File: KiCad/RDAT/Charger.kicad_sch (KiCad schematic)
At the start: 52 parts, among them U6 BQ24617RGER

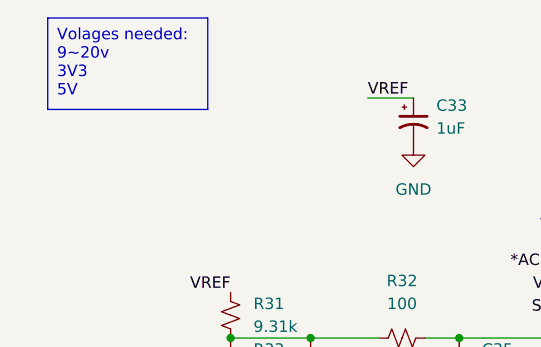
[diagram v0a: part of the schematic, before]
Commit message: Add new notes; update component references in schematics and footprints, and complete charging design
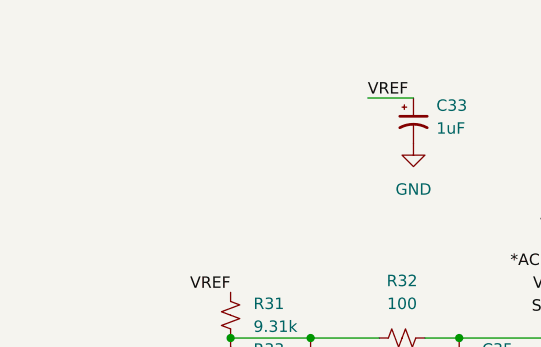
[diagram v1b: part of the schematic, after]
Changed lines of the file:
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@@
 		)
 	)
-	(text_box "Volages needed:\n9~20v\n3V3\n5V"
-		(exclude_from_sim no)
-		(at 15.24 15.24 0)
-		(size 17.78 10.16)
-		(stroke
-			(width 0)
-			(type default)
-		)
-		(fill
-			(type none)
-		)
-		(effects
-			(font
-				(size 1.27 1.27)
-			)
-			(justify left top)
-		)
-	)
 	(text "Q2"
 		(exclude_from_sim no)
@@
 		)
 		(instances
-			(project ""
+			(project "RDAT"
 				(path "/0db9370a-8a21-4fd2-83a9-f207c3725dc9/64601ab1-4b63-421f-a3b9-e484b74e1409"
 					(reference "#PWR052")
@@
 		)
 		(instances
-			(project ""
+			(project "RDAT"
 				(path "/0db9370a-8a21-4fd2-83a9-f207c3725dc9/64601ab1-4b63-421f-a3b9-e484b74e1409"
 					(reference "C35")
@@
 		)
 		(instances
-			(project ""
+			(project "RDAT"
 				(path "/0db9370a-8a21-4fd2-83a9-f207c3725dc9/64601ab1-4b63-421f-a3b9-e484b74e1409"
 					(reference "C42")
@@
 		)
 		(instances
-			(project ""
+			(project "RDAT"
 				(path "/0db9370a-8a21-4fd2-83a9-f207c3725dc9/64601ab1-4b63-421f-a3b9-e484b74e1409"
 					(reference "U6")
@@
 		)
 		(instances
-			(project ""
+			(project "RDAT"
 				(path "/0db9370a-8a21-4fd2-83a9-f207c3725dc9/64601ab1-4b63-421f-a3b9-e484b74e1409"
 					(reference "D111")
@@
 		)
 		(instances
-			(project ""
+			(project "RDAT"
 				(path "/0db9370a-8a21-4fd2-83a9-f207c3725dc9/64601ab1-4b63-421f-a3b9-e484b74e1409"
 					(reference "#PWR051")
@@
 		)
 		(instances
-			(project ""
+			(project "RDAT"
 				(path "/0db9370a-8a21-4fd2-83a9-f207c3725dc9/64601ab1-4b63-421f-a3b9-e484b74e1409"
 					(reference "C36")
@@
 		)
 		(instances
-			(project ""
+			(project "RDAT"
 				(path "/0db9370a-8a21-4fd2-83a9-f207c3725dc9/64601ab1-4b63-421f-a3b9-e484b74e1409"
 					(reference "#PWR050")
@@
 		)
 		(instances
-			(project ""
+			(project "RDAT"
 				(path "/0db9370a-8a21-4fd2-83a9-f207c3725dc9/64601ab1-4b63-421f-a3b9-e484b74e1409"
 					(reference "R33")
@@
 		)
 		(instances
-			(project ""
+			(project "RDAT"
 				(path "/0db9370a-8a21-4fd2-83a9-f207c3725dc9/64601ab1-4b63-421f-a3b9-e484b74e1409"
 					(reference "R32")
@@
 		)
 		(instances
-			(project ""
+			(project "RDAT"
 				(path "/0db9370a-8a21-4fd2-83a9-f207c3725dc9/64601ab1-4b63-421f-a3b9-e484b74e1409"
 					(reference "R43")
@@
 		)
 		(instances
-			(project ""
+			(project "RDAT"
 				(path "/0db9370a-8a21-4fd2-83a9-f207c3725dc9/64601ab1-4b63-421f-a3b9-e484b74e1409"
 					(reference "#PWR053")
@@
 		)
 		(instances
-			(project ""
+			(project "RDAT"
 				(path "/0db9370a-8a21-4fd2-83a9-f207c3725dc9/64601ab1-4b63-421f-a3b9-e484b74e1409"
 					(reference "R45")
@@
 		)
 		(instances
-			(project ""
+			(project "RDAT"
 				(path "/0db9370a-8a21-4fd2-83a9-f207c3725dc9/64601ab1-4b63-421f-a3b9-e484b74e1409"
 					(reference "R47")
@@
 		)
 		(instances
-			(project ""
+			(project "RDAT"
 				(path "/0db9370a-8a21-4fd2-83a9-f207c3725dc9/64601ab1-4b63-421f-a3b9-e484b74e1409"
 					(reference "R46")
@@
 		)
 		(instances
-			(project ""
+			(project "RDAT"
 				(path "/0db9370a-8a21-4fd2-83a9-f207c3725dc9/64601ab1-4b63-421f-a3b9-e484b74e1409"
 					(reference "R_{SR}")
@@
 		)
 		(instances
-			(project ""
+			(project "RDAT"
 				(path "/0db9370a-8a21-4fd2-83a9-f207c3725dc9/64601ab1-4b63-421f-a3b9-e484b74e1409"
 					(reference "D114")
@@
 		)
 		(instances
-			(project ""
+			(project "RDAT"
 				(path "/0db9370a-8a21-4fd2-83a9-f207c3725dc9/64601ab1-4b63-421f-a3b9-e484b74e1409"
 					(reference "TH2")
@@
 		)
 		(instances
-			(project ""
+			(project "RDAT"
 				(path "/0db9370a-8a21-4fd2-83a9-f207c3725dc9/64601ab1-4b63-421f-a3b9-e484b74e1409"
 					(reference "D113")
@@
 		)
 		(instances
-			(project ""
+			(project "RDAT"
 				(path "/0db9370a-8a21-4fd2-83a9-f207c3725dc9/64601ab1-4b63-421f-a3b9-e484b74e1409"
 					(reference "L1")
@@
 		)
 		(instances
-			(project ""
+			(project "RDAT"
 				(path "/0db9370a-8a21-4fd2-83a9-f207c3725dc9/64601ab1-4b63-421f-a3b9-e484b74e1409"
 					(reference "R44")
@@
 		)
 		(instances
-			(project ""
+			(project "RDAT"
 				(path "/0db9370a-8a21-4fd2-83a9-f207c3725dc9/64601ab1-4b63-421f-a3b9-e484b74e1409"
 					(reference "#PWR060")
@@
 		)
 		(instances
-			(project ""
+			(project "RDAT"
 				(path "/0db9370a-8a21-4fd2-83a9-f207c3725dc9/64601ab1-4b63-421f-a3b9-e484b74e1409"
 					(reference "C38")
@@
 		)
 		(instances
-			(project ""
+			(project "RDAT"
 				(path "/0db9370a-8a21-4fd2-83a9-f207c3725dc9/64601ab1-4b63-421f-a3b9-e484b74e1409"
 					(reference "C34")
@@
 		)
 		(instances
-			(project ""
+			(project "RDAT"
 				(path "/0db9370a-8a21-4fd2-83a9-f207c3725dc9/64601ab1-4b63-421f-a3b9-e484b74e1409"
 					(reference "D112")
@@
 		)
 		(instances
-			(project ""
+			(project "RDAT"
 				(path "/0db9370a-8a21-4fd2-83a9-f207c3725dc9/64601ab1-4b63-421f-a3b9-e484b74e1409"
 					(reference "MOSFET3")
@@
 		)
 		(instances
-			(project ""
+			(project "RDAT"
 				(path "/0db9370a-8a21-4fd2-83a9-f207c3725dc9/64601ab1-4b63-421f-a3b9-e484b74e1409"
 					(reference "R31")

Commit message: added volage stuffs
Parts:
- renumbered R_{AC} to R_{AC}1, R_{SR} to R_{SR}1
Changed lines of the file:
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@@
 (kicad_sch
-	(version 20231120)
+	(version 20250114)
 	(generator "eeschema")
-	(generator_version "8.0")
+	(generator_version "9.0")
 	(paper "USLetter" portrait)
 	(title_block
 		(rev "0")
 	)
+	(text "Q2"
+		(exclude_from_sim no)
+		(at 187.706 153.416 0)
+		(effects
+			(font
+				(size 1.27 1.27)
+			)
+		)
+	)
+	(text "Q1"
+		(exclude_from_sim no)
+		(at 53.594 212.598 0)
+		(effects
+			(font
+				(size 1.27 1.27)
+			)
+		)
+	)
+	(text "Q1"
+		(exclude_from_sim no)
+		(at 114.554 212.598 0)
+		(effects
+			(font
+				(size 1.27 1.27)
+			)
+		)
+	)
 	(junction
 		(at 149.86 66.04)
@@
 		)
 	)
-	(text "Q2"
-		(exclude_from_sim no)
-		(at 187.706 153.416 0)
-		(effects
-			(font
-				(size 1.27 1.27)
-			)
-		)
-	)
-	(text "Q1"
-		(exclude_from_sim no)
-		(at 53.594 212.598 0)
-		(effects
-			(font
-				(size 1.27 1.27)
-			)
-		)
-	)
-	(text "Q1"
-		(exclude_from_sim no)
-		(at 114.554 212.598 0)
-		(effects
-			(font
-				(size 1.27 1.27)
-			)
-		)
-	)
 	(label "PH"
 		(at 129.54 172.72 0)
@@
 		(on_board yes)
 		(dnp no)
-		(property "Reference" "R_{AC}"
+		(property "Reference" "R_{AC}1"
 			(at 156.21 195.5801 0)
 			(effects
@@
 			(project "RDAT"
 				(path "/0db9370a-8a21-4fd2-83a9-f207c3725dc9/64601ab1-4b63-421f-a3b9-e484b74e1409"
-					(reference "R_{AC}")
+					(reference "R_{AC}1")
 					(unit 1)
 				)
@@
 		(dnp no)
 		(fields_autoplaced yes)
-		(property "Reference" "R_{SR}"
+		(property "Reference" "R_{SR}1"
 			(at 148.59 163.83 90)
 			(effects
@@
 			(project "RDAT"
 				(path "/0db9370a-8a21-4fd2-83a9-f207c3725dc9/64601ab1-4b63-421f-a3b9-e484b74e1409"
-					(reference "R_{SR}")
+					(reference "R_{SR}1")
 					(unit 1)
 				)

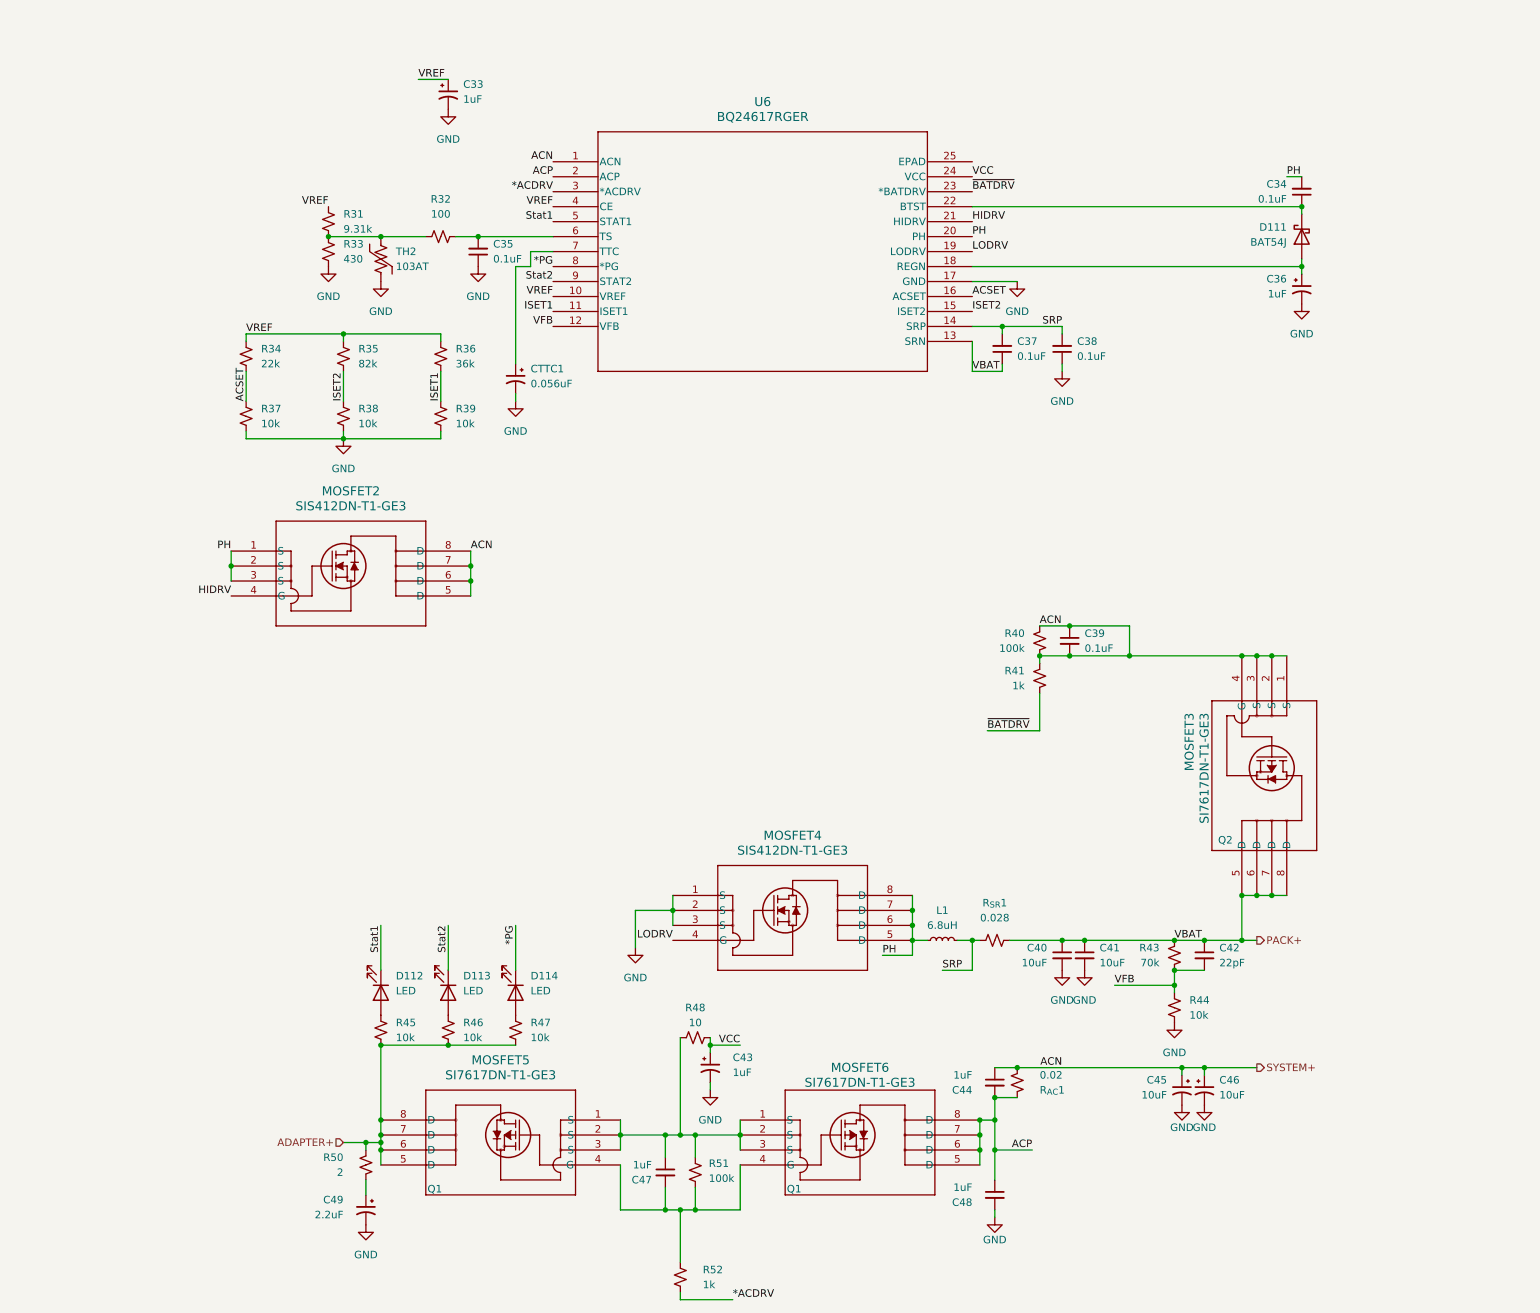
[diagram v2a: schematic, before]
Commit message: Modified Power Stages
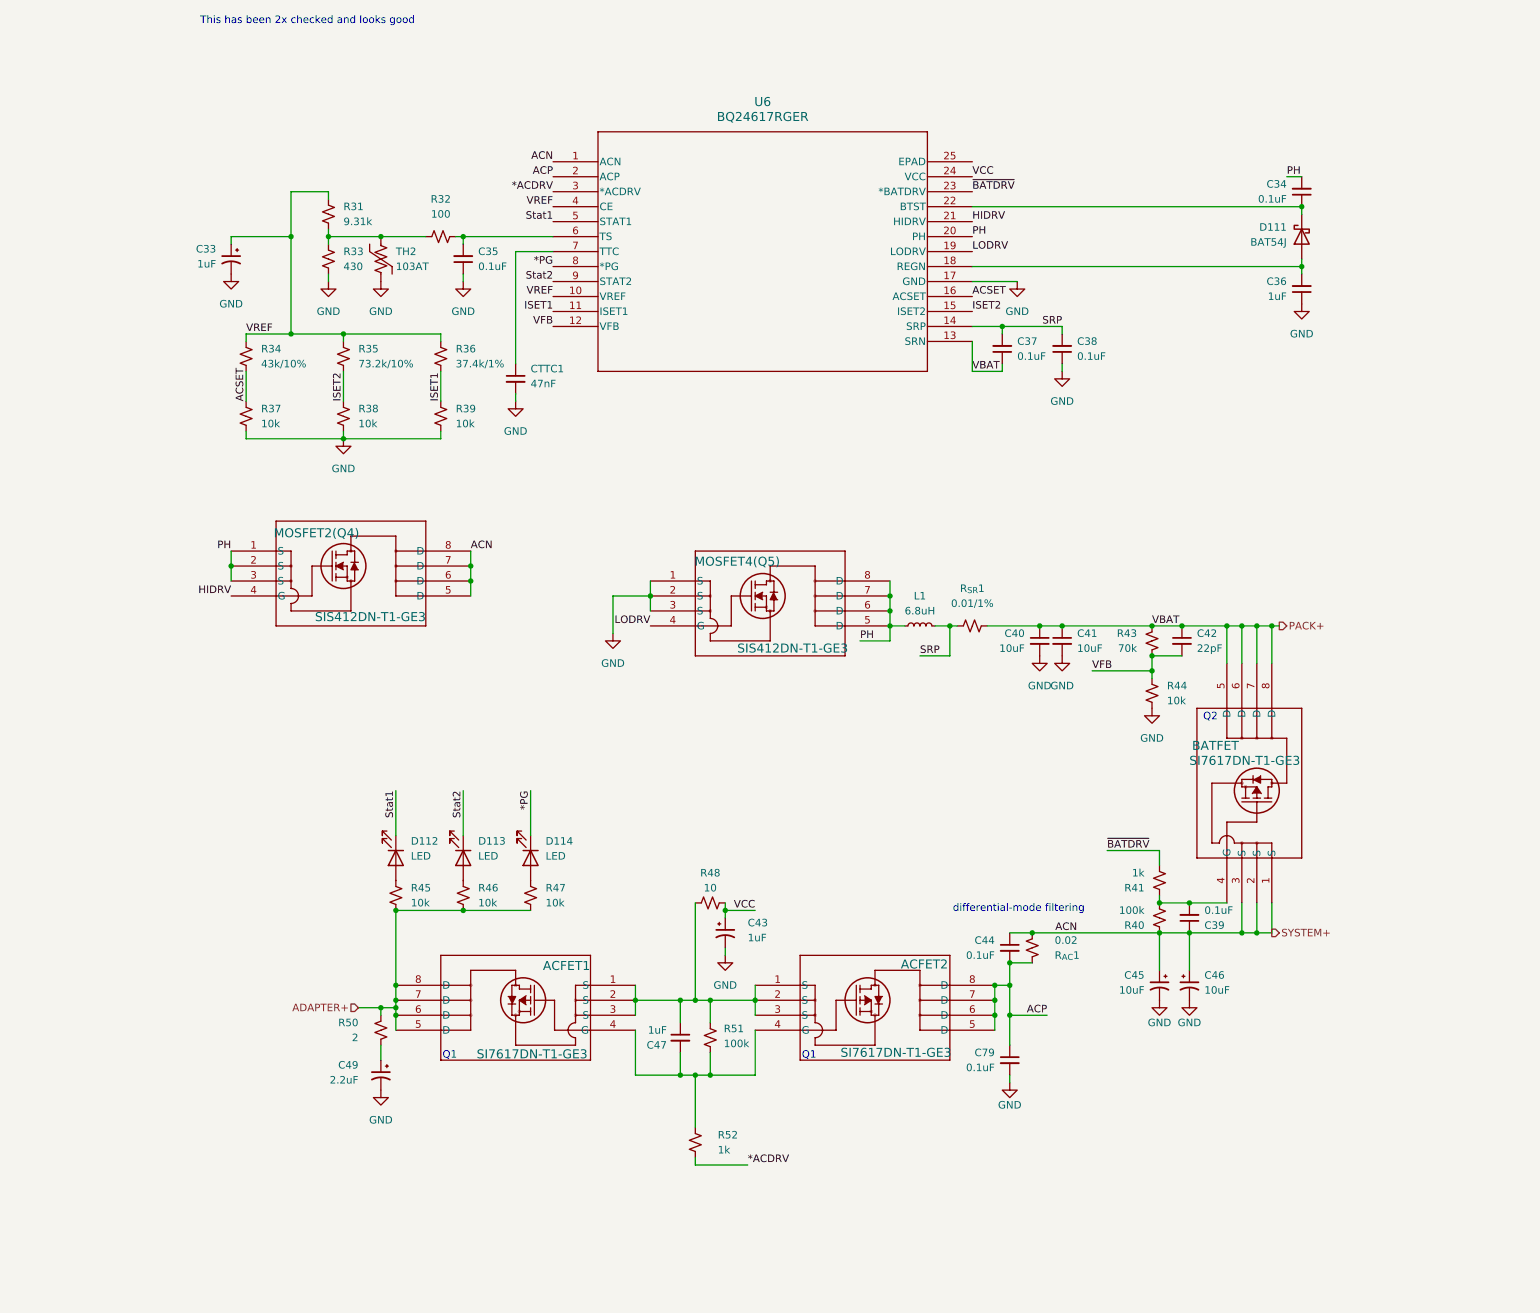
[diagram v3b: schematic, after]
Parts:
- removed C36: 1uF, symbol Device:C_Polarized_Small_US
- removed C48: 1uF, symbol Device:C_Small
- added C36: 1uF, symbol Device:C_Small
- added C79: 0.1uF, symbol Device:C_Small
- C44: value 1uF -> 0.1uF
- CTTC1: value 0.056uF -> 47nF; symbol Device:C_Polarized_Small_US -> Device:C_Small
- R34: value 22k -> 43k/10%
- R35: value 82k -> 73.2k/10%
- R36: value 36k -> 37.4k/1%
- R_{SR}1: value 0.028 -> 0.01/1%
- renumbered MOSFET5 to ACFET1, MOSFET6 to ACFET2, MOSFET3 to BATFET, MOSFET2 to MOSFET2(Q4), MOSFET4 to MOSFET4(Q5)
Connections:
- net ACP: now also C79.1
- net GND: now also C36.1, C79.2
- net SYSTEM+: no longer BATFET.4 (G), C39.2, R40.2, R41.1
- net at D111.2 (A), U6.18 (REGN): now also C36.2
- new net: BATFET.4 (G), C39.2, R40.2, R41.1
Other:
- note added: "This has been 2x checked and looks good"
- note added: "differential-mode filtering"
- moved on the sheet: ACFET1, ACFET2, BATFET, C33, C35, C39, C40, C41, C42, C43, C44, C45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

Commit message: Pre-Annotate FULL, add usb
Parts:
- ACFET1, ACFET2, BATFET: JLCPCB_LINK (none) -> https://jlcpcb.com/partdetail/VishayIntertech-SI7617DN_T1GE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
